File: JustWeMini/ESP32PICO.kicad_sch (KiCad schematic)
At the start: 8 parts, among them J1 Conn_01x06, U1 ESP32-PICO-D4

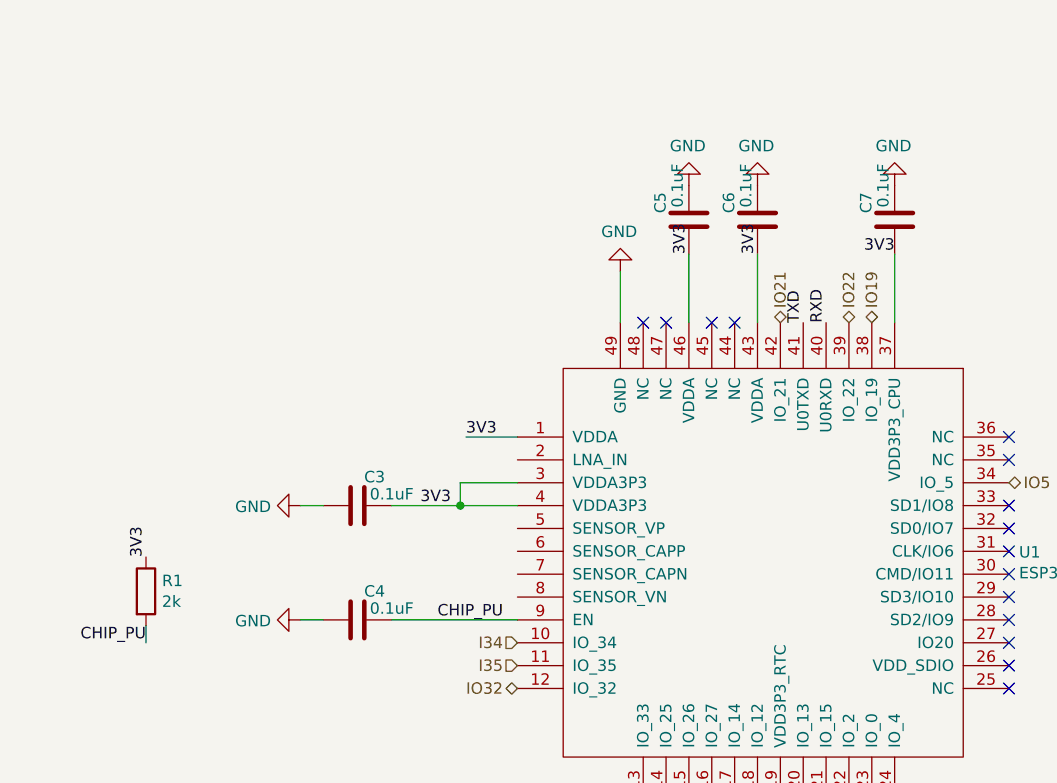
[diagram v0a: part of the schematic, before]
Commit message: Feat: MPN adjusted
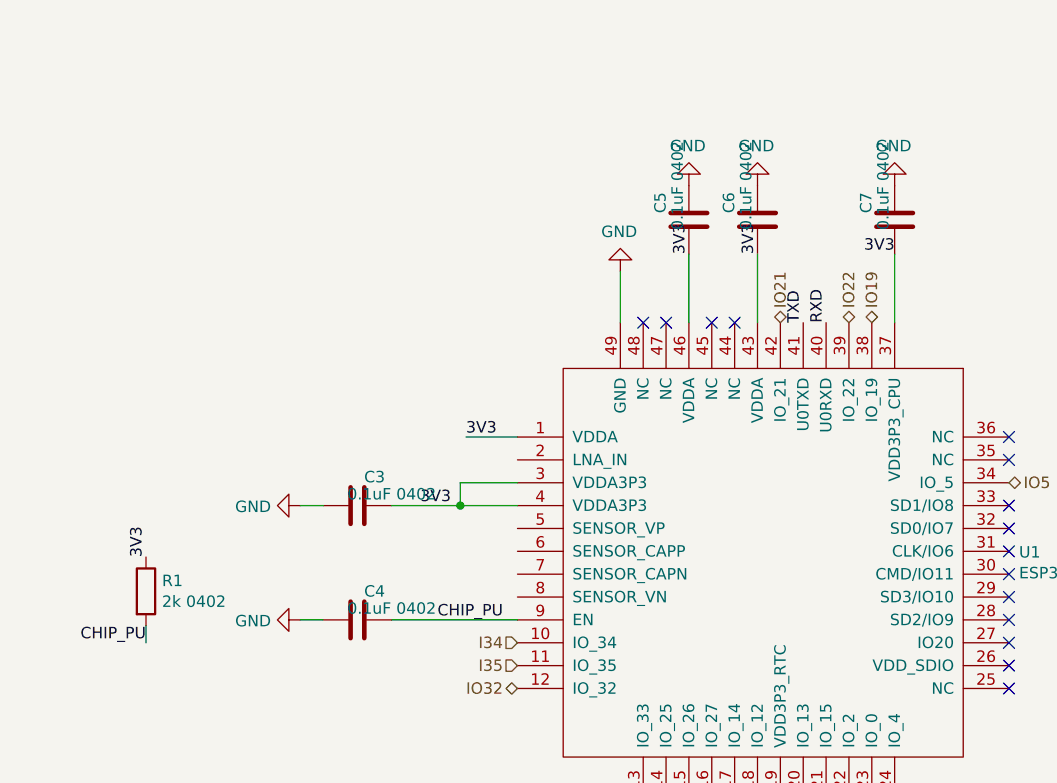
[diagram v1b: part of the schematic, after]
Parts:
- C3, C4, C5, C6, C7: value 0.1uF -> 0.1uF 0402; MPN (none) -> CL05F104ZO5NNND
- J1: MPN (none) -> 440054-6
- R1: value 2k -> 2k 0402; MPN (none) -> CR0402-JW-202GLF
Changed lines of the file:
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@@
       (effects (font (size 1.27 1.27)) (justify left))
     )
-    (property "Value" "2k" (id 1) (at 65.3288 75.946 0)
+    (property "Value" "2k 0402" (id 1) (at 65.3288 75.946 0)
       (effects (font (size 1.27 1.27)) (justify left))
     )
@@
       (effects (font (size 1.27 1.27)) hide)
     )
-    (property "Datasheet" "~" (id 3) (at 63.5508 74.803 0)
-      (effects (font (size 1.27 1.27)) hide)
-    )
-    (property "MPN" "" (id 4) (at 63.5508 74.803 0)
+    (property "Datasheet" "" (id 3) (at 63.5508 74.803 0)
+      (effects (font (size 1.27 1.27)) hide)
+    )
+    (property "MPN" "CR0402-JW-202GLF" (id 4) (at 63.5508 74.803 0)
       (effects (font (size 1.27 1.27)) hide)
     )
@@
     (in_bom yes) (on_board yes)
     (property "Reference" "C7" (id 0) (at 143.5608 31.623 90))
-    (property "Value" "0.1uF" (id 1) (at 145.4658 29.718 90))
+    (property "Value" "0.1uF 0402" (id 1) (at 145.4658 29.718 90))
     (property "Footprint" "Capacitor_SMD:C_0402_1005Metric" (id 2) (at 145.7706 29.718 0)
       (effects (font (size 1.27 1.27)) hide)
     )
-    (property "Datasheet" "~" (id 3) (at 146.7358 33.528 0)
-      (effects (font (size 1.27 1.27)) hide)
-    )
-    (property "MPN" "" (id 4) (at 146.7358 33.528 0)
+    (property "Datasheet" "" (id 3) (at 146.7358 33.528 0)
+      (effects (font (size 1.27 1.27)) hide)
+    )
+    (property "MPN" "CL05F104ZO5NNND" (id 4) (at 146.7358 33.528 0)
       (effects (font (size 1.27 1.27)) hide)
     )
@@
     (in_bom yes) (on_board yes)
     (property "Reference" "C5" (id 0) (at 120.7008 31.623 90))
-    (property "Value" "0.1uF" (id 1) (at 122.6058 29.718 90))
+    (property "Value" "0.1uF 0402" (id 1) (at 122.6058 29.718 90))
     (property "Footprint" "Capacitor_SMD:C_0402_1005Metric" (id 2) (at 122.9106 29.718 0)
       (effects (font (size 1.27 1.27)) hide)
     )
-    (property "Datasheet" "~" (id 3) (at 123.8758 33.528 0)
-      (effects (font (size 1.27 1.27)) hide)
-    )
-    (property "MPN" "" (id 4) (at 123.8758 33.528 0)
+    (property "Datasheet" "" (id 3) (at 123.8758 33.528 0)
+      (effects (font (size 1.27 1.27)) hide)
+    )
+    (property "MPN" "CL05F104ZO5NNND" (id 4) (at 123.8758 33.528 0)
       (effects (font (size 1.27 1.27)) hide)
     )
@@
       (effects (font (size 1.27 1.27)) hide)
     )
-    (property "MPN" "" (id 4) (at 31.3436 26.2128 0)
+    (property "MPN" "440054-6" (id 4) (at 31.3436 26.2128 0)
       (effects (font (size 1.27 1.27)) hide)
     )
@@
     (in_bom yes) (on_board yes)
     (property "Reference" "C4" (id 0) (at 88.9508 74.803 90))
-    (property "Value" "0.1uF" (id 1) (at 90.8558 76.708 90))
+    (property "Value" "0.1uF 0402" (id 1) (at 90.8558 76.708 90))
     (property "Footprint" "Capacitor_SMD:C_0402_1005Metric" (id 2) (at 90.8558 77.0128 0)
       (effects (font (size 1.27 1.27)) hide)
     )
-    (property "Datasheet" "~" (id 3) (at 87.0458 77.978 0)
-      (effects (font (size 1.27 1.27)) hide)
-    )
-    (property "MPN" "" (id 4) (at 87.0458 77.978 0)
+    (property "Datasheet" "" (id 3) (at 87.0458 77.978 0)
+      (effects (font (size 1.27 1.27)) hide)
+    )
+    (property "MPN" "CL05F104ZO5NNND" (id 4) (at 87.0458 77.978 0)
       (effects (font (size 1.27 1.27)) hide)
     )
@@
     (in_bom yes) (on_board yes)
     (property "Reference" "C6" (id 0) (at 128.3208 31.623 90))
-    (property "Value" "0.1uF" (id 1) (at 130.2258 29.718 90))
+    (property "Value" "0.1uF 0402" (id 1) (at 130.2258 29.718 90))
     (property "Footprint" "Capacitor_SMD:C_0402_1005Metric" (id 2) (at 130.5306 29.718 0)
       (effects (font (size 1.27 1.27)) hide)
     )
-    (property "Datasheet" "~" (id 3) (at 131.4958 33.528 0)
-      (effects (font (size 1.27 1.27)) hide)
-    )
-    (property "MPN" "" (id 4) (at 131.4958 33.528 0)
+    (property "Datasheet" "" (id 3) (at 131.4958 33.528 0)
+      (effects (font (size 1.27 1.27)) hide)
+    )
+    (property "MPN" "CL05F104ZO5NNND" (id 4) (at 131.4958 33.528 0)
       (effects (font (size 1.27 1.27)) hide)
     )
@@
     (in_bom yes) (on_board yes)
     (property "Reference" "C3" (id 0) (at 88.9508 62.103 90))
-    (property "Value" "0.1uF" (id 1) (at 90.8558 64.008 90))
+    (property "Value" "0.1uF 0402" (id 1) (at 90.8558 64.008 90))
     (property "Footprint" "Capacitor_SMD:C_0402_1005Metric" (id 2) (at 90.8558 64.3128 0)
       (effects (font (size 1.27 1.27)) hide)
     )
-    (property "Datasheet" "~" (id 3) (at 87.0458 65.278 0)
-      (effects (font (size 1.27 1.27)) hide)
-    )
-    (property "MPN" "" (id 4) (at 87.0458 65.278 0)
-      (effects (font (size 1.27 1.27)) hide)
-    )
+    (property "Datasheet" "" (id 3) (at 87.0458 65.278 0)
+      (effects (font (size 1.27 1.27)) hide)
+    )
+    (property "MPN" "CL05F104ZO5NNND" (id 4) (at 87.0458 65.278 0)
+      (effects (font (size 1.27 1.27)) hide)
+    )
